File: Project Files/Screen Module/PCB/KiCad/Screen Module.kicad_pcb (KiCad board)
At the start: 2 copper layers, 70 x 116 mm, 21 parts, among them J1 Conn_01x19_Male, J2 Conn_01x19_Male, J3 Conn_02x04_Top_Bottom, J4 Conn_02x03_Top_Bottom, Q1 BC817, SW1 SW_Push, SW2 SW_Push

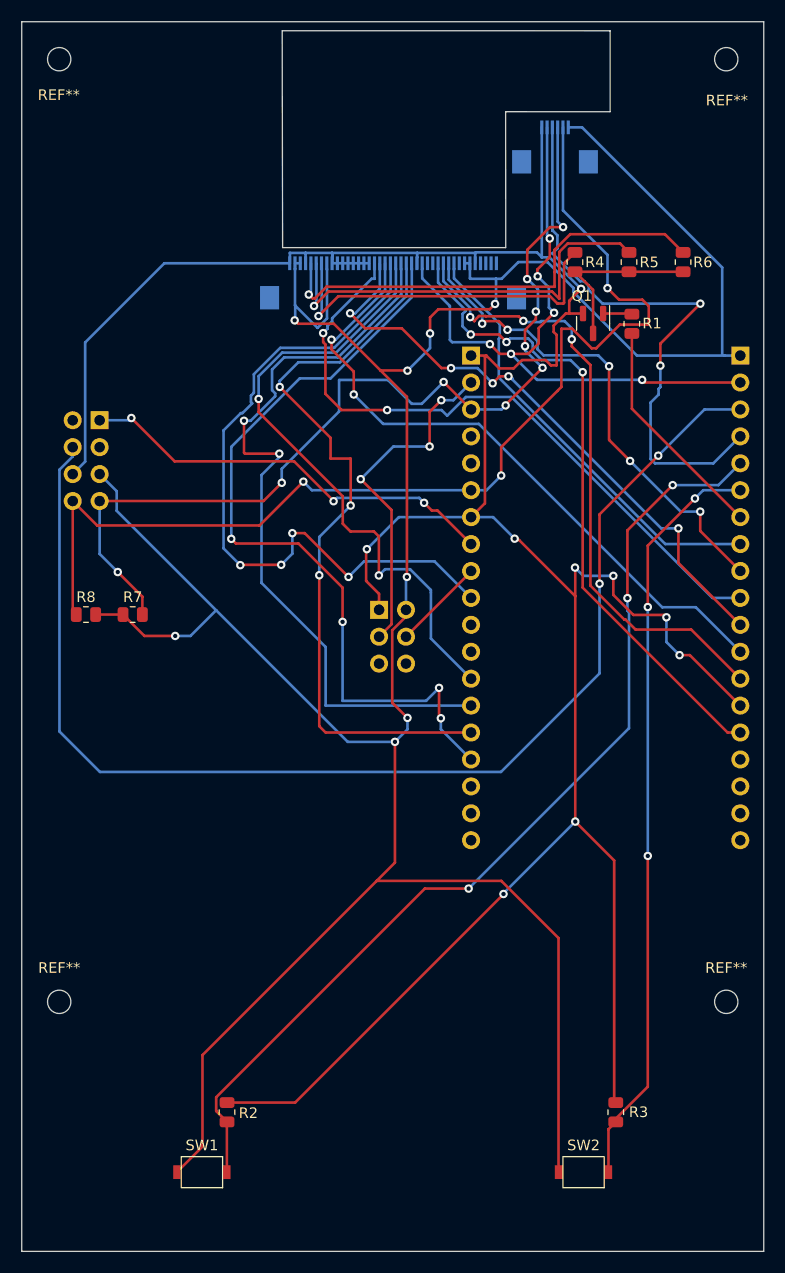
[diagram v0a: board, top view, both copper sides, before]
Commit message: Updated PCB to fix several issues Wall Module: Fixed relay flyback diodes pointing in the wrong direction.
Screen PCB:
Fixed display LED resistors to be a more suitable value.
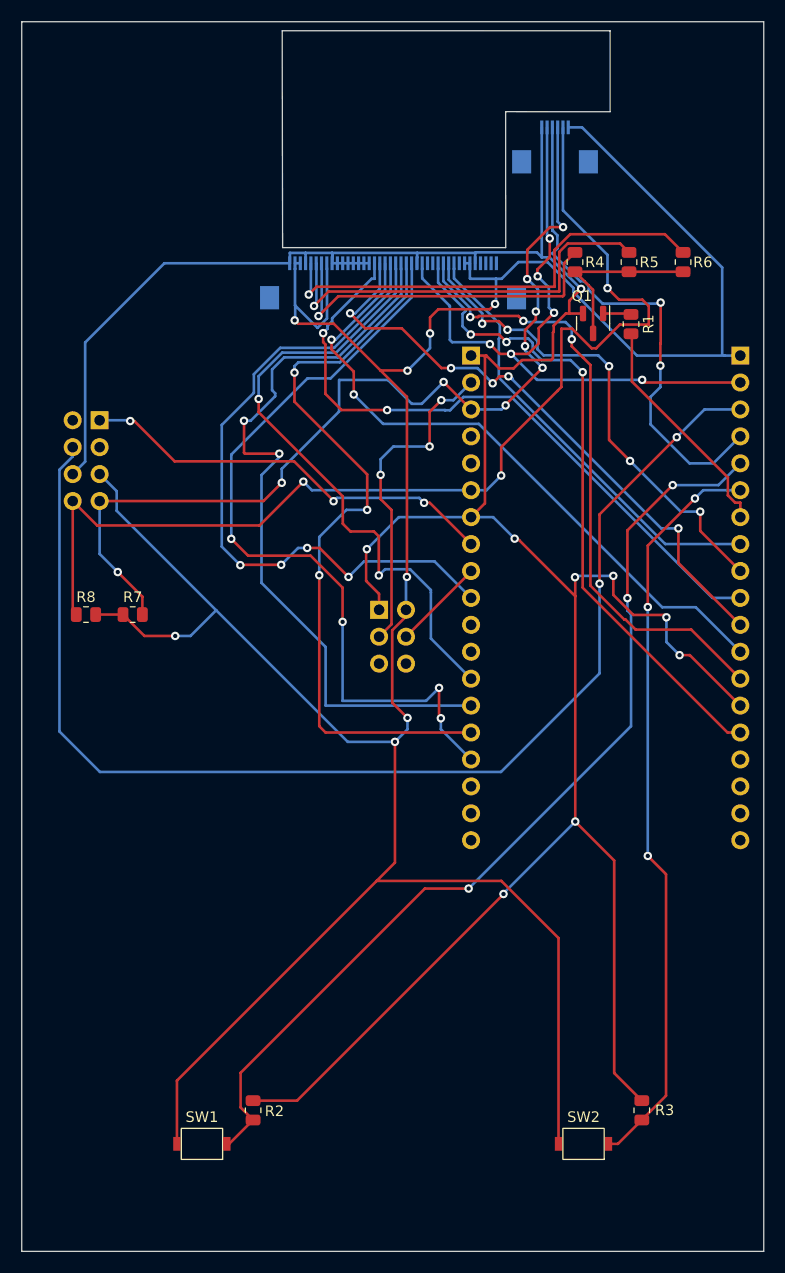
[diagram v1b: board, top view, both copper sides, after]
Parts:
- removed REF** (x4): MountingHole_2.2mm_M2, MountingHole:MountingHole_2.2mm_M2
- R1: value 10K -> 100
- R4, R5, R6: value 10 -> 100
- moved SW1 2.67 mm to (77.6, 134.5)
- moved SW2 2.67 mm to (113.6, 134.5)
- moved R2 2.46 mm to (82.5, 133.9)
- moved R3 2.46 mm to (119.1, 133.9)
- moved R1 0.09 mm to (118.1, 59.7), turned to -90 degrees
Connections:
- R1 pad 1: TFT_Backlight -> Net-(Q1-Pad1)
- R1 pad 2: Net-(Q1-Pad1) -> TFT_Backlight
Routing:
- net CTC_IRQ: track 54.7 -> 47.7 mm
- net 3.3V: track 283.0 -> 277.7 mm
- net GND: track 270.3 -> 266.2 mm
- net DB4: track 66.2 -> 63.9 mm
- net BTN1: track 92.9 -> 90.6 mm
- net RELAY2T: track 32.7 -> 31.1 mm
- net LED_K1: track 34.0 -> 33.0 mm
- net LED_K2: track 39.8 -> 38.8 mm
- net BTN2: track 71.5 -> 70.8 mm
